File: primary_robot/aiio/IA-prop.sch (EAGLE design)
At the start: 43 parts, among them U1 ARDUINO_R3_SHIELD

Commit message: [primary_robot] Fixes Uart2 to Uart1 on the BBB
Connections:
- removed net RX2_BBB: CON_I2C_UART.6, U$3P9.GPIO_2
- removed net TX2_BBB: CON_I2C_UART.5, U$3P9.GPIO_3
- new net RX1_BBB: CON_I2C_UART.6, U$3P9.GPIO_14
- new net TX1_BBB: CON_I2C_UART.5, U$3P9.GPIO_15
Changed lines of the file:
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@@
-</segment>
-</net>
-<net name="TX2_BBB" class="0">
-<segment>
-<pinref part="U$3" gate="P9" pin="GPIO_3"/>
-<wire x1="10.16" y1="-109.22" x2="5.08" y2="-109.22" width="0.1524" layer="91"/>
-<label x="-5.08" y="-109.22" size="1.778" layer="95"/>
-</segment>
-<segment>
-<pinref part="CON_I2C_UART" gate="G$1" pin="5"/>
-<wire x1="144.78" y1="-99.06" x2="142.24" y2="-99.06" width="0.1524" layer="91"/>
-<label x="132.08" y="-99.06" size="1.778" layer="95"/>
-</segment>
-</net>
-<net name="RX2_BBB" class="0">
-<segment>
-<pinref part="U$3" gate="P9" pin="GPIO_2"/>
-<wire x1="50.8" y1="-109.22" x2="55.88" y2="-109.22" width="0.1524" layer="91"/>
-<label x="55.88" y="-109.22" size="1.778" layer="95"/>
-</segment>
-<segment>
-<pinref part="CON_I2C_UART" gate="G$1" pin="6"/>
-<wire x1="144.78" y1="-101.6" x2="142.24" y2="-101.6" width="0.1524" layer="91"/>
-<label x="132.08" y="-101.6" size="1.778" layer="95"/>
 </segment>
 </net>
@@
 </segment>
 </net>
+<net name="TX1_BBB" class="0">
+<segment>
+<pinref part="U$3" gate="P9" pin="GPIO_15"/>
+<wire x1="50.8" y1="-111.76" x2="55.88" y2="-111.76" width="0.1524" layer="91"/>
+<label x="55.88" y="-111.76" size="1.778" layer="95"/>
+</segment>
+<segment>
+<pinref part="CON_I2C_UART" gate="G$1" pin="5"/>
+<wire x1="144.78" y1="-99.06" x2="142.24" y2="-99.06" width="0.1524" layer="91"/>
+<label x="132.08" y="-99.06" size="1.778" layer="95"/>
+</segment>
+</net>
+<net name="RX1_BBB" class="0">
+<segment>
+<pinref part="U$3" gate="P9" pin="GPIO_14"/>
+<wire x1="50.8" y1="-114.3" x2="55.88" y2="-114.3" width="0.1524" layer="91"/>
+<label x="55.88" y="-114.3" size="1.778" layer="95"/>
+</segment>
+<segment>
+<pinref part="CON_I2C_UART" gate="G$1" pin="6"/>
+<wire x1="144.78" y1="-101.6" x2="142.24" y2="-101.6" width="0.1524" layer="91"/>
+<label x="132.08" y="-101.6" size="1.778" layer="95"/>
+</segment>
+</net>

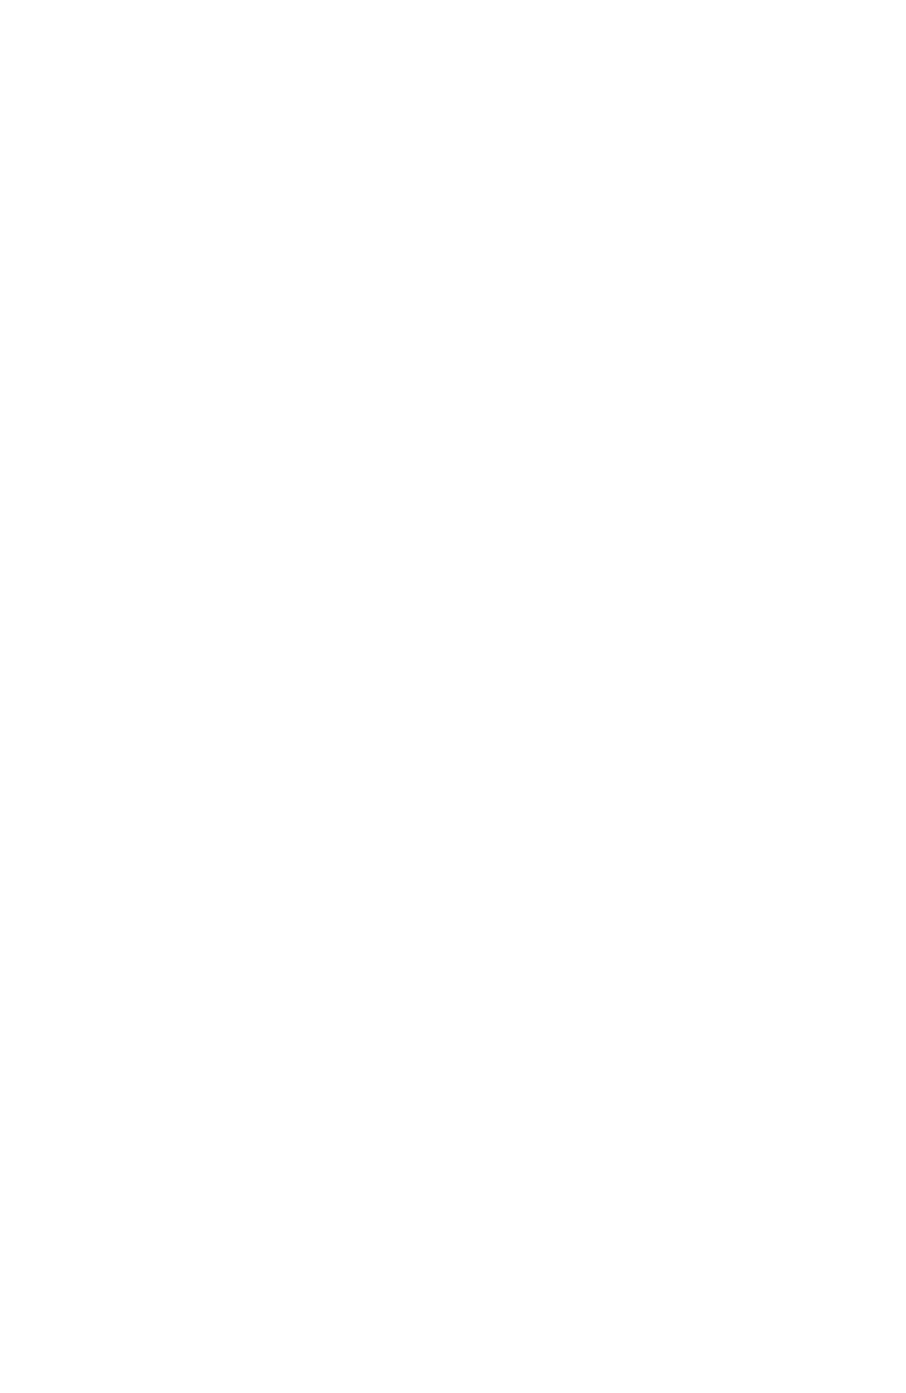
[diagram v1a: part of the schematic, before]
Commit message: [AIIO_board] Add I2C bus "I2C0" for sonar sensors on shematic file.
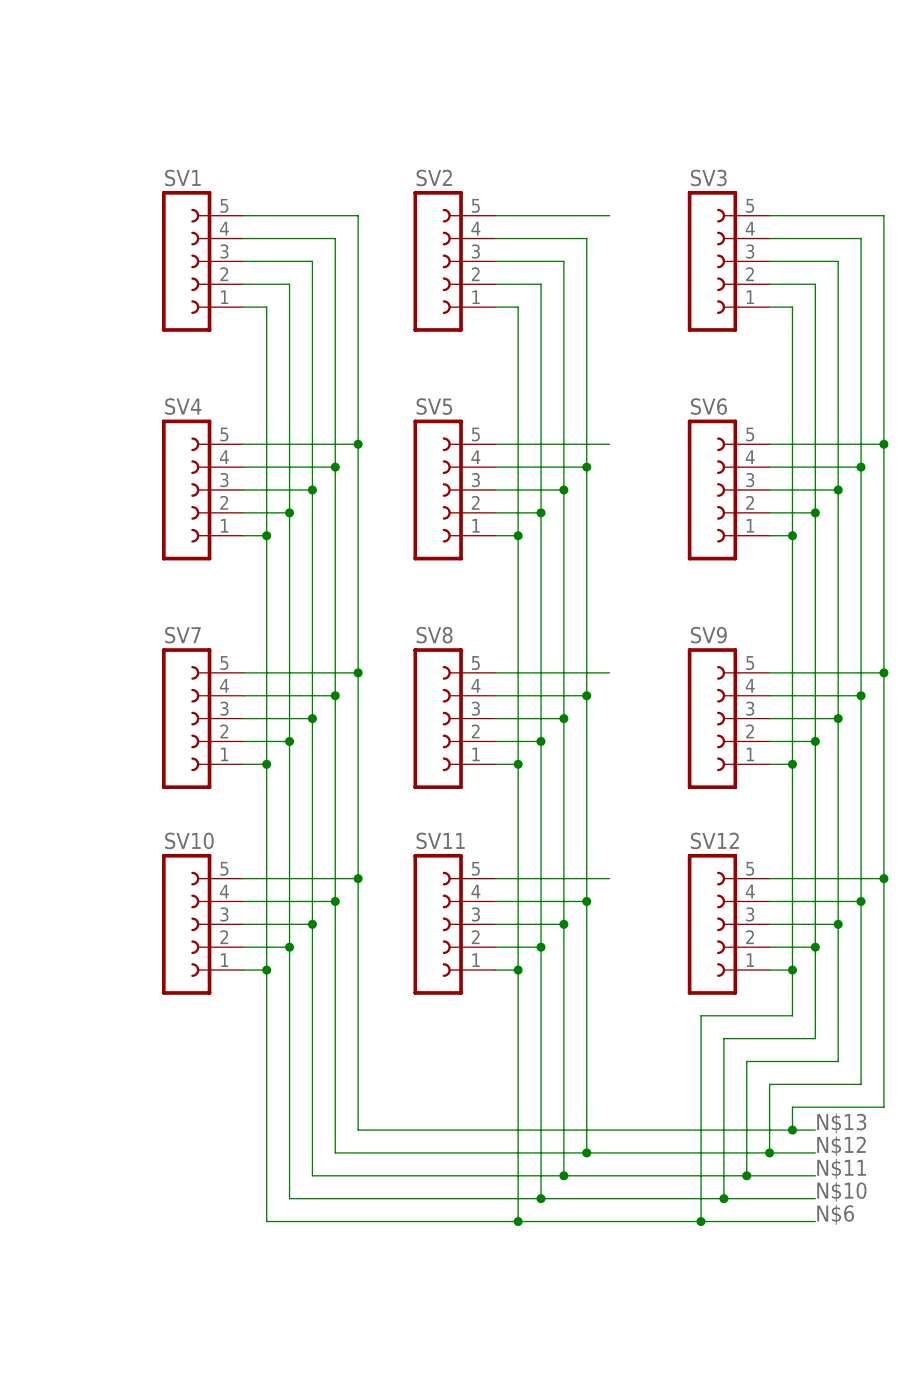
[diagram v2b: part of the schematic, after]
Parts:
- added SV1, SV10, SV11, SV12, SV2, SV3, SV4, SV5, SV6, SV7, SV8, SV9: (no value), con-lsta:FE05-1
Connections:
- new net N$10: SV1.2, SV10.2, SV11.2, SV12.2, SV2.2, SV3.2, SV4.2, SV5.2, SV6.2, SV7.2, SV8.2, SV9.2
- new net N$11: SV1.3, SV10.3, SV11.3, SV12.3, SV2.3, SV3.3, SV4.3, SV5.3, SV6.3, SV7.3, SV8.3, SV9.3
- new net N$12: SV1.4, SV10.4, SV11.4, SV12.4, SV2.4, SV3.4, SV4.4, SV5.4, SV6.4, SV7.4, SV8.4, SV9.4
- new net N$13: SV1.5, SV10.5, SV12.5, SV3.5, SV4.5, SV6.5, SV7.5, SV9.5
- new net N$23: SV5.5
- new net N$38: SV8.5
- new net N$48: SV2.5
- new net N$6: SV1.1, SV10.1, SV11.1, SV12.1, SV2.1, SV3.1, SV4.1, SV5.1, SV6.1, SV7.1, SV8.1, SV9.1
- new net N$63: SV11.5
